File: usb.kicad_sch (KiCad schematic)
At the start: 3 parts, among them J19 USB_C_Receptacle_USB2.0_14P

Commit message: finish initial supporting components for mcu
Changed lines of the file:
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@@
+	(wire
+		(pts
+			(xy 0.0762 20.3962) (xy 16.5862 20.3962)
+		)
+		(stroke
+			(width 0)
+			(type default)
+		)
+	)
 	(wire
 		(pts
@@
 	(wire
 		(pts
+			(xy 0.0762 0.0762) (xy 0.0762 20.3962)
+		)
+		(stroke
+			(width 0)
+			(type default)
+		)
+	)
+	(wire
+		(pts
 			(xy 88.9 66.04) (xy 92.71 66.04)
 		)
@@
 		)
 		(stroke
+			(width 0)
+			(type default)
+		)
+	)
+	(wire
+		(pts
+			(xy 16.5862 20.3962) (xy 16.5862 24.2062)
+		)
+		(stroke

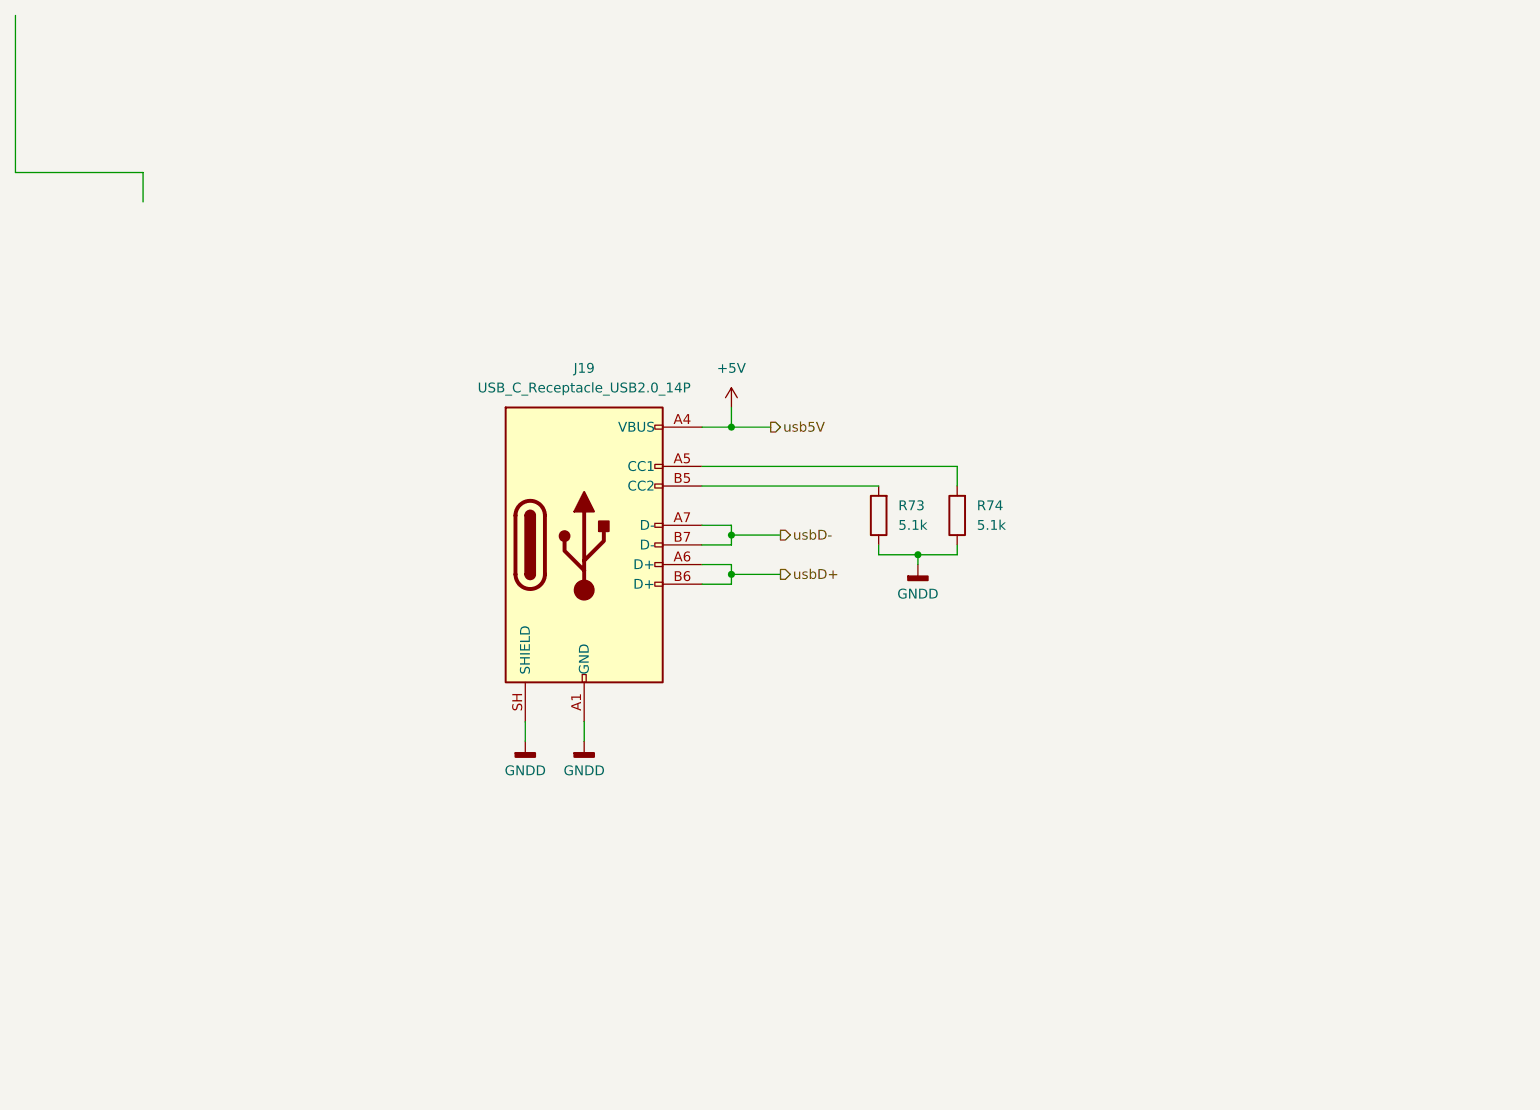
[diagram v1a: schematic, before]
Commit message: fix nearly all erc errors
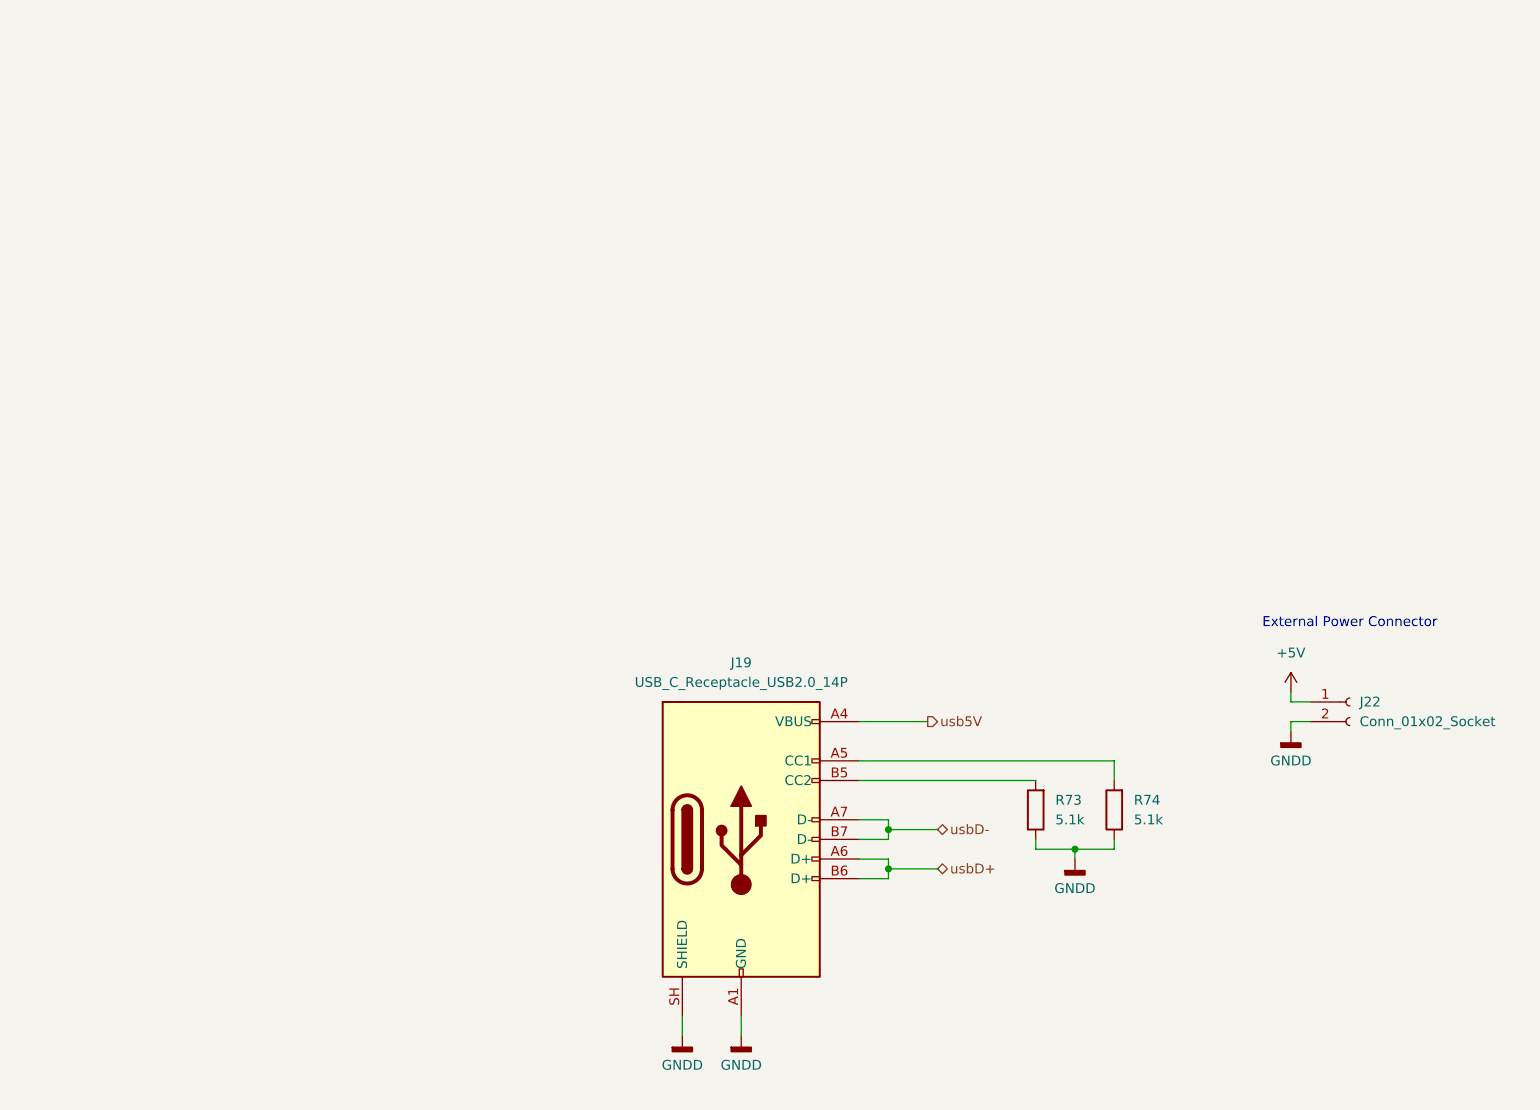
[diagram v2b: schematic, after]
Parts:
- added J22: Conn_01x02_Socket, symbol Connector:Conn_01x02_Socket
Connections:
- net +5V: now also J22.1 (Pin_1); no longer J19.A4 (VBUS), J19.A9 (VBUS), J19.B4 (VBUS), J19.B9 (VBUS)
- net GNDD: now also J22.2 (Pin_2)
- new net usb5V: J19.A4 (VBUS), J19.A9 (VBUS), J19.B4 (VBUS), J19.B9 (VBUS)
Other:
- note added: "External Power Connector"
- moved on the sheet: J19, R73, R74

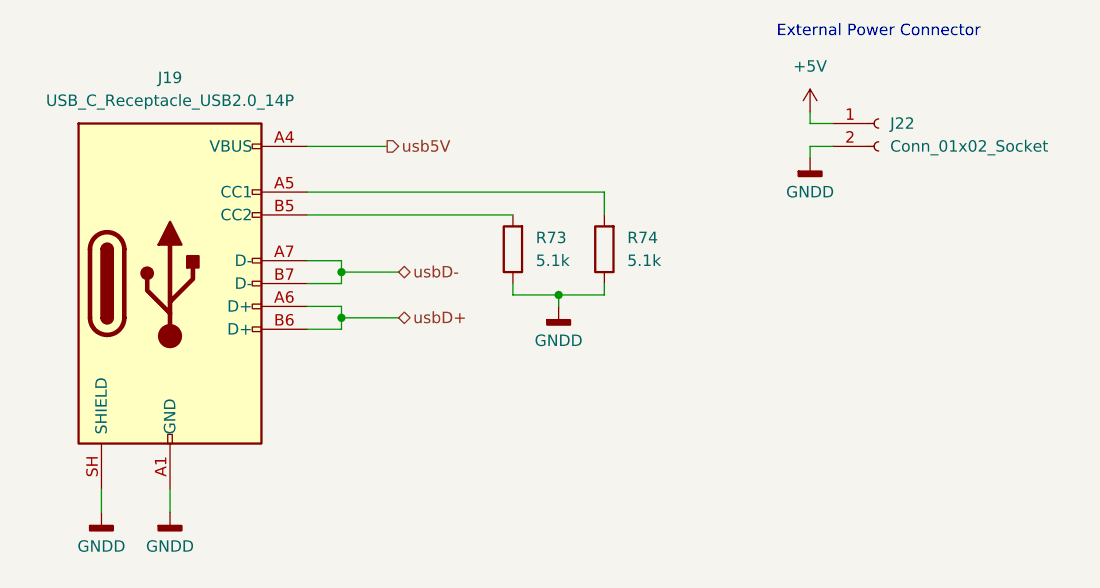
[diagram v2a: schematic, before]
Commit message: unsplit grounds, finish power circuitry, start picking footprints/partnumbers
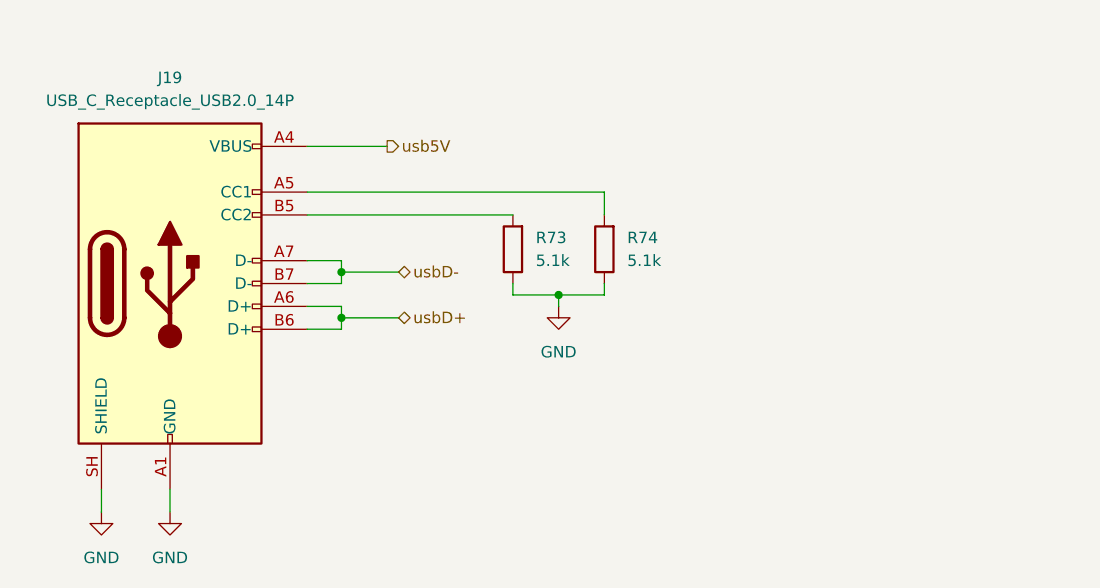
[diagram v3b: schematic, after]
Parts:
- removed J22: Conn_01x02_Socket, symbol Connector:Conn_01x02_Socket
- J19: footprint (none) -> Connector_USB:USB_C_Receptacle_Amphenol_12401610E4-2A; DKPN (none) -> 12401610E4#2ACT-ND
- R73, R74: footprint (none) -> Resistor_SMD:R_0805_2012Metric
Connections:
- net GNDD renamed GND
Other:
- note removed: "External Power Connector"

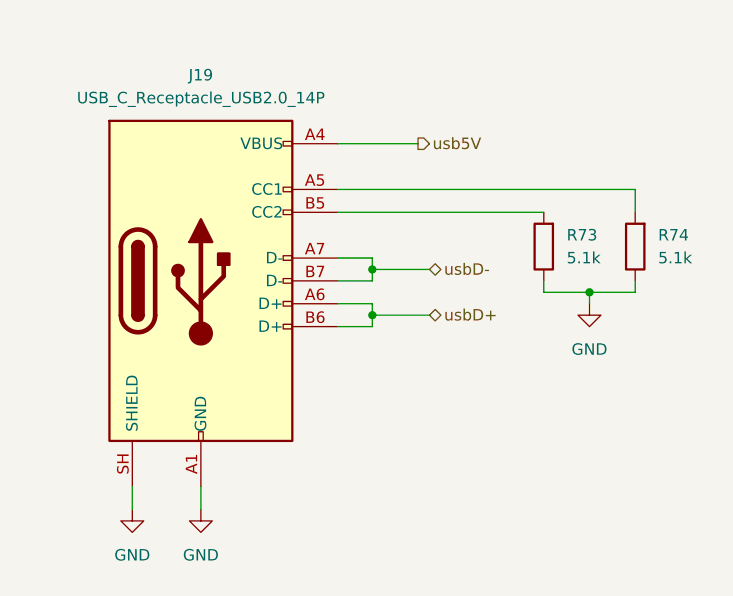
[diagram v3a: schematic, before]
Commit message: added power mux, finished up schematic and picking footprints/partnumbers
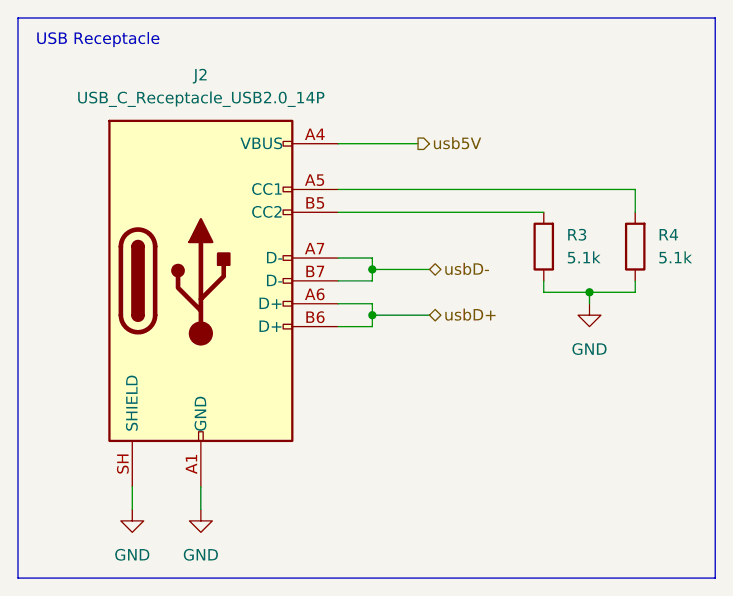
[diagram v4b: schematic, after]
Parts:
- renumbered J19 to J2, R73 to R3, R74 to R4
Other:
- note added: "USB Receptacle"
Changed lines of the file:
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@@
 		(comment 4 "Tobe Cynar")
+	)
+	(rectangle
+		(start 73.66 77.47)
+		(end 151.13 139.7)
+		(stroke
+			(width 0)
+			(type default)
+		)
+		(fill
+			(type none)
+		)
+	)
+	(text "USB Receptacle"
+		(exclude_from_sim no)
+		(at 82.55 80.01 0)
+		(effects
+			(font
+				(size 1.27 1.27)
+			)
+		)
 	)
 	(junction
@@
 		(dnp no)
 		(fields_autoplaced yes)
-		(property "Reference" "#PWR4"
+		(property "Reference" "#PWR017"
 			(at 137.16 115.57 0)
 			(hide yes)
@@
 			(project "pbx-sniffer-v2"
 				(path "/eb421281-26a1-483f-b39a-0425ec8eb8df/09b79dd0-426f-45f8-8b40-abaa4f7beb7c"
-					(reference "#PWR4")
+					(reference "#PWR017")
 					(unit 1)
 				)
@@
 		(dnp no)
 		(fields_autoplaced yes)
-		(property "Reference" "R73"
+		(property "Reference" "R3"
 			(at 134.62 101.5999 0)
 			(show_name no)
@@
 			(project "pbx-sniffer-v2"
 				(path "/eb421281-26a1-483f-b39a-0425ec8eb8df/09b79dd0-426f-45f8-8b40-abaa4f7beb7c"
-					(reference "R73")
+					(reference "R3")
 					(unit 1)
 				)
@@
 		(dnp no)
 		(fields_autoplaced yes)
-		(property "Reference" "#PWR3"
+		(property "Reference" "#PWR015"
 			(at 86.36 138.43 0)
 			(hide yes)
@@
 			(project "pbx-sniffer-v2"
 				(path "/eb421281-26a1-483f-b39a-0425ec8eb8df/09b79dd0-426f-45f8-8b40-abaa4f7beb7c"
-					(reference "#PWR3")
+					(reference "#PWR015")
 					(unit 1)
 				)
@@
 		(dnp no)
 		(fields_autoplaced yes)
-		(property "Reference" "J19"
+		(property "Reference" "J2"
 			(at 93.98 83.82 0)
 			(show_name no)
@@
 			(project "pbx-sniffer-v2"
 				(path "/eb421281-26a1-483f-b39a-0425ec8eb8df/09b79dd0-426f-45f8-8b40-abaa4f7beb7c"
-					(reference "J19")
+					(reference "J2")
 					(unit 1)
 				)
@@
 		(dnp no)
 		(fields_autoplaced yes)
-		(property "Reference" "#PWR2"
+		(property "Reference" "#PWR016"
 			(at 93.98 138.43 0)
 			(hide yes)
@@
 			(project "pbx-sniffer-v2"
 				(path "/eb421281-26a1-483f-b39a-0425ec8eb8df/09b79dd0-426f-45f8-8b40-abaa4f7beb7c"
-					(reference "#PWR2")
+					(reference "#PWR016")
 					(unit 1)
 				)
@@
 		(dnp no)
 		(fields_autoplaced yes)
-		(property "Reference" "R74"
+		(property "Reference" "R4"
 			(at 144.78 101.5999 0)
 			(show_name no)
@@
 			(project "pbx-sniffer-v2"
 				(path "/eb421281-26a1-483f-b39a-0425ec8eb8df/09b79dd0-426f-45f8-8b40-abaa4f7beb7c"
-					(reference "R74")
+					(reference "R4")
 					(unit 1)
 				)
